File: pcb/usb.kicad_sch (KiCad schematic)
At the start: 8 parts, among them J2 Same Sky UJ20-C-H-G-SMT-P16-TR, U4 USBLC6-2SC6

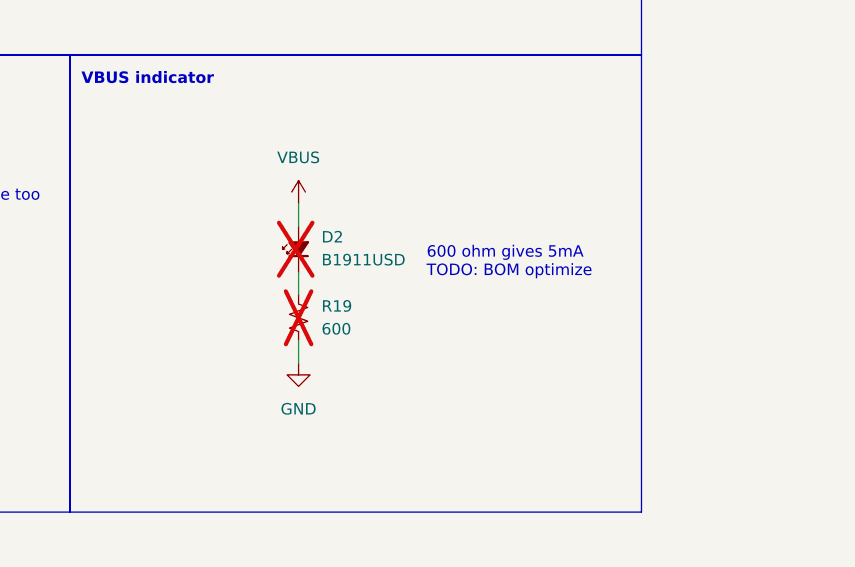
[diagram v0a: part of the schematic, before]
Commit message: Enabled and implemented VBUS LED
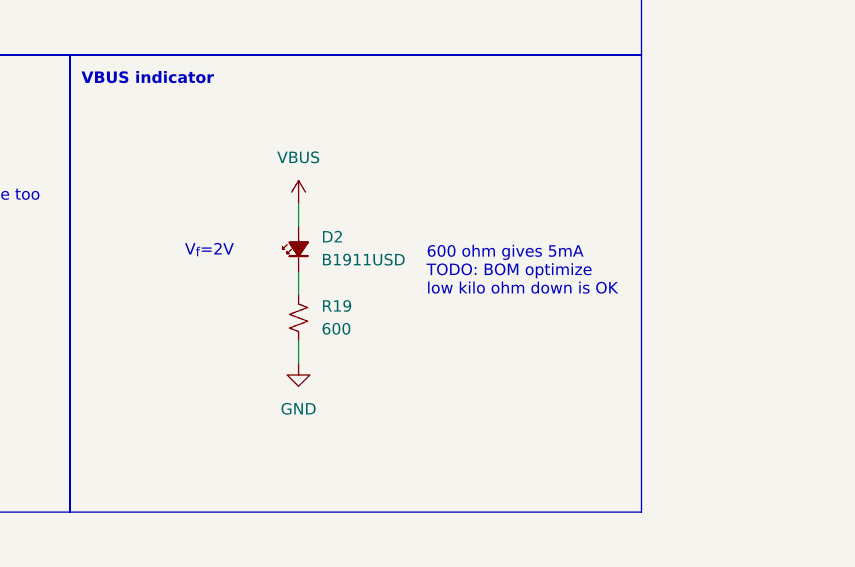
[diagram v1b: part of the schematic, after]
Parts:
- D2, R19: now fitted
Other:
- note added: "600 ohm gives 5mA TODO: BOM optimize low kilo ohm down is OK"
- note added: "V_{f}=2V"
- note removed: "600 ohm gives 5mA TODO: BOM optimize"
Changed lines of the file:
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@@
 		)
 	)
-	(text "600 ohm gives 5mA\nTODO: BOM optimize"
+	(text "600 ohm gives 5mA\nTODO: BOM optimize\nlow kilo ohm down is OK"
 		(exclude_from_sim no)
 		(at 103.124 122.936 0)
@@
 		(exclude_from_sim no)
 		(at 44.45 117.348 0)
+		(effects
+			(font
+				(size 1.27 1.27)
+			)
+		)
+	)
+	(text "V_{f}=2V"
+		(exclude_from_sim no)
+		(at 78.994 123.444 0)
 		(effects
 			(font
@@
 		(exclude_from_sim no)
 		(in_bom yes)
-		(on_board no)
-		(dnp yes)
+		(on_board yes)
+		(dnp no)
 		(fields_autoplaced yes)
 		(property "Reference" "R19"
@@
 		(exclude_from_sim no)
 		(in_bom yes)
-		(on_board no)
-		(dnp yes)
+		(on_board yes)
+		(dnp no)
 		(fields_autoplaced yes)
 		(property "Reference" "D2"

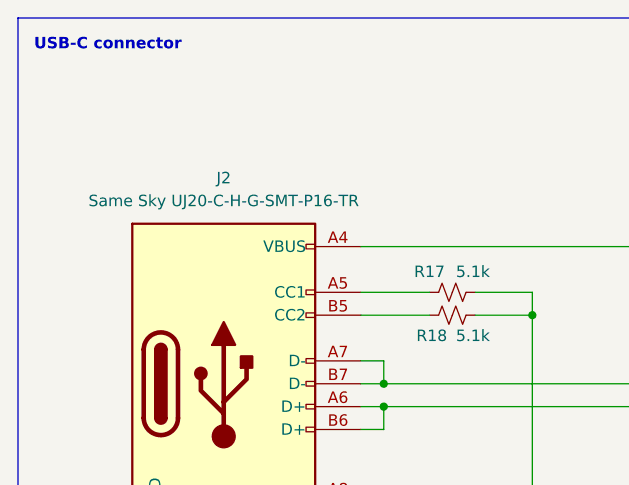
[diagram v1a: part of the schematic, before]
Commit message: Add MPN field for components except resistors
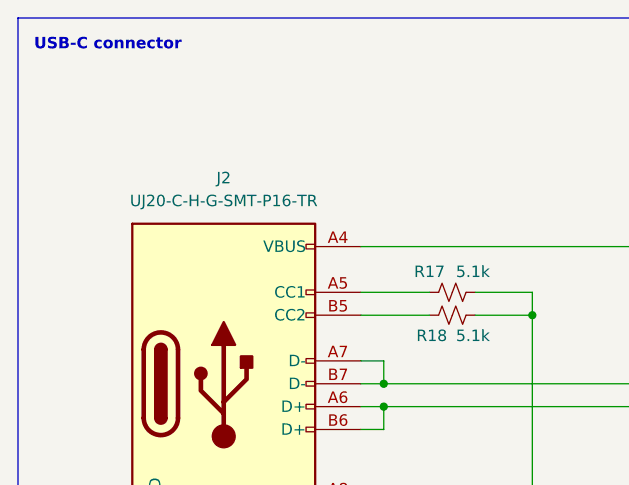
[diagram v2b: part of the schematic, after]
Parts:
- D2: MPN (none) -> B1911USD-20D000114U1930
- J2: value Same Sky UJ20-C-H-G-SMT-P16-TR -> UJ20-C-H-G-SMT-P16-TR; MPN (none) -> UJ20-C-H-G-SMT-P16-TR
- U4: MPN (none) -> USBLC6-2SC6
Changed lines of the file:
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@@
+			)
+		)
+		(property "MPN" ""
+			(at 88.9 130.81 0)
+			(effects
+				(font
+					(size 1.27 1.27)
+				)
+				(hide yes)
 			)
 		)
@@
 			)
 		)
+		(property "MPN" ""
+			(at 60.96 43.18 90)
+			(effects
+				(font
+					(size 1.27 1.27)
+				)
+				(hide yes)
+			)
+		)
 		(pin "1"
 		)
@@
 			)
 		)
+		(property "MPN" "B1911USD-20D000114U1930"
+			(at 88.9 123.19 90)
+			(effects
+				(font
+					(size 1.27 1.27)
+				)
+				(hide yes)
+			)
+		)
 		(pin "2"
 		)
@@
 			)
 		)
-		(property "Value" "Same Sky UJ20-C-H-G-SMT-P16-TR"
+		(property "Value" "UJ20-C-H-G-SMT-P16-TR"
 			(at 35.56 33.02 0)
 			(effects
@@
 			)
 		)
+		(property "MPN" "UJ20-C-H-G-SMT-P16-TR"
+			(at 35.56 53.34 0)
+			(effects
+				(font
+					(size 1.27 1.27)
+				)
+				(hide yes)
+			)
+		)
 		(pin "B6"
 		)
@@
 			)
 		)
+		(property "MPN" ""
+			(at 60.96 45.72 90)
+			(effects
+				(font
+					(size 1.27 1.27)
+				)
+				(hide yes)
+			)
+		)
 		(pin "1"
 		)
@@
 			)
 		)
+		(property "MPN" ""
+			(at 25.4 121.92 0)
+			(effects
+				(font
+					(size 1.27 1.27)
+				)
+				(hide yes)
+			)
+		)
 		(pin "2"
 		)
@@
 			)
 		)
+		(property "MPN" "USBLC6-2SC6"
+			(at 88.9 53.34 0)
+			(effects
+				(font
+					(size 1.27 1.27)
+				)
+				(hide yes)
+			)
+		)
 		(pin "6"
 		)
@@
 			(at 25.4 132.08 0)
 			(effects
+				(font
+					(size 1.27 1.27)
+				)
+				(hide yes)
+			)
+		)
+		(property "MPN" ""
+			(at 25.4 132.08 0)
+			(effects

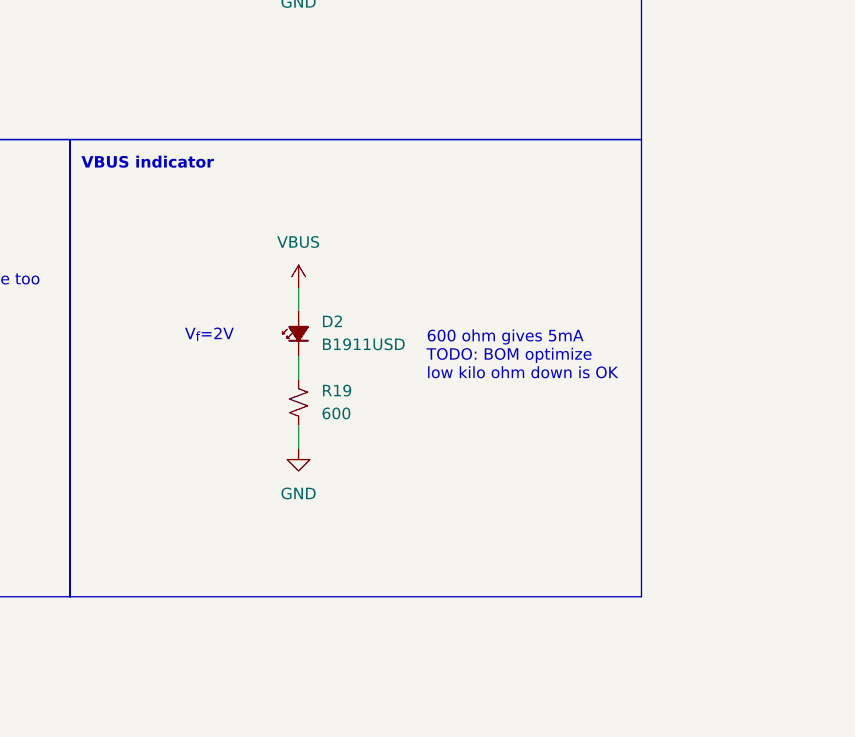
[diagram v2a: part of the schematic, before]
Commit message: BOM optimize VBUS LED
600R to 3x 150R = 450R for 6.667 mA
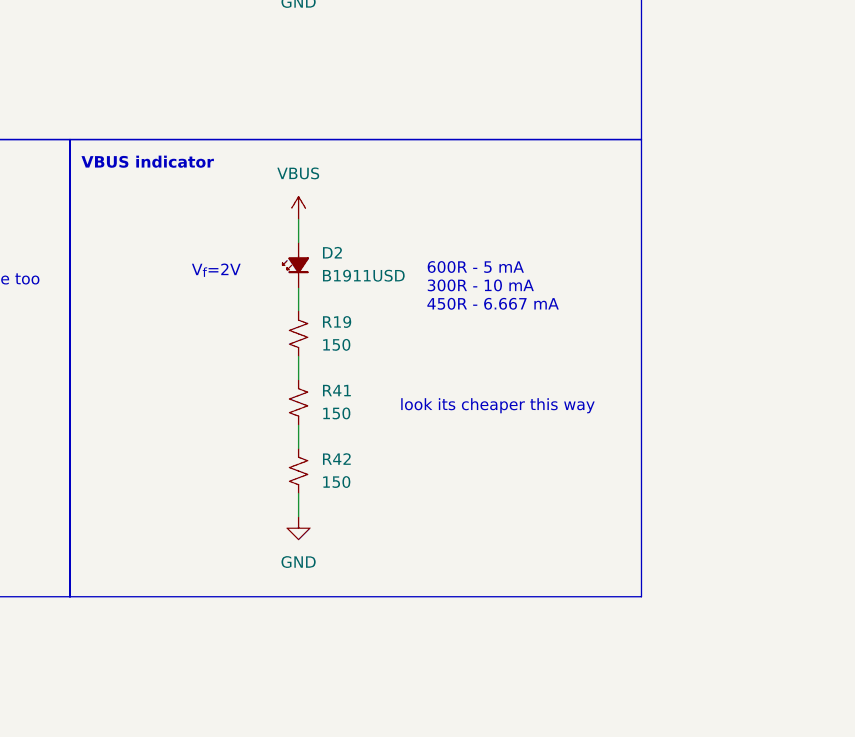
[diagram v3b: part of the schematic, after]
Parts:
- added R41, R42: 150, Resistor_SMD:R_0603_1608Metric, symbol Device:R_Small_US
- R19: value 600 -> 150
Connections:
- net GND: now also R42.2; no longer R19.2
- new net: R19.2, R41.1
- new net: R41.2, R42.1
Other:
- note added: "600R - 5 mA 300R - 10 mA 450R - 6.667 mA"
- note added: "look its cheaper this way"
- note removed: "600 ohm gives 5mA TODO: BOM optimize low kilo ohm down is OK"
- moved on the sheet: D2, R19

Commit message: Update resistor MPNs
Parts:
- R15: MPN (none) -> AC0603FR-0730KL
- R16: MPN (none) -> RC0603FR-0747KL
- R17, R18: MPN (none) -> RC0603FR-075K1L
- R19, R41, R42: MPN (none) -> RC0603JR-07150RL
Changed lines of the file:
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@@
 			)
 		)
-		(property "MPN" ""
+		(property "MPN" "RC0603JR-07150RL"
 			(at 88.9 123.19 0)
 			(effects
@@
 			)
 		)
-		(property "MPN" ""
+		(property "MPN" "RC0603FR-075K1L"
 			(at 60.96 43.18 90)
 			(effects
@@
 			)
 		)
-		(property "MPN" ""
+		(property "MPN" "RC0603FR-075K1L"
 			(at 60.96 45.72 90)
 			(effects
@@
 			)
 		)
-		(property "MPN" ""
+		(property "MPN" "AC0603FR-0730KL"
 			(at 25.4 121.92 0)
 			(effects
@@
 			)
 		)
-		(property "MPN" ""
+		(property "MPN" "RC0603JR-07150RL"
 			(at 88.9 130.81 0)
 			(effects
@@
 			)
 		)
-		(property "MPN" ""
+		(property "MPN" "RC0603JR-07150RL"
 			(at 88.9 138.43 0)
 			(effects
@@
 			)
 		)
-		(property "MPN" ""
+		(property "MPN" "RC0603FR-0747KL"
 			(at 25.4 132.08 0)
 			(effects

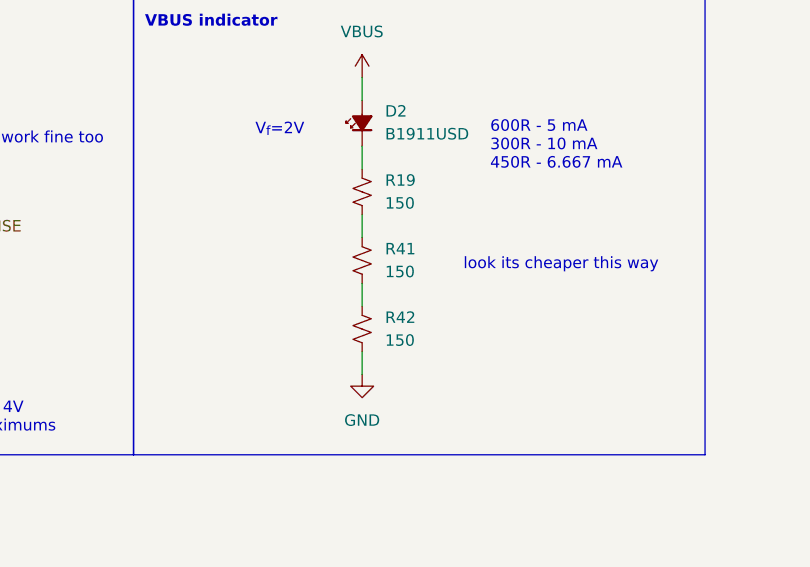
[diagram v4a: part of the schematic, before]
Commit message: Redo layout and routing for RGB LEDs
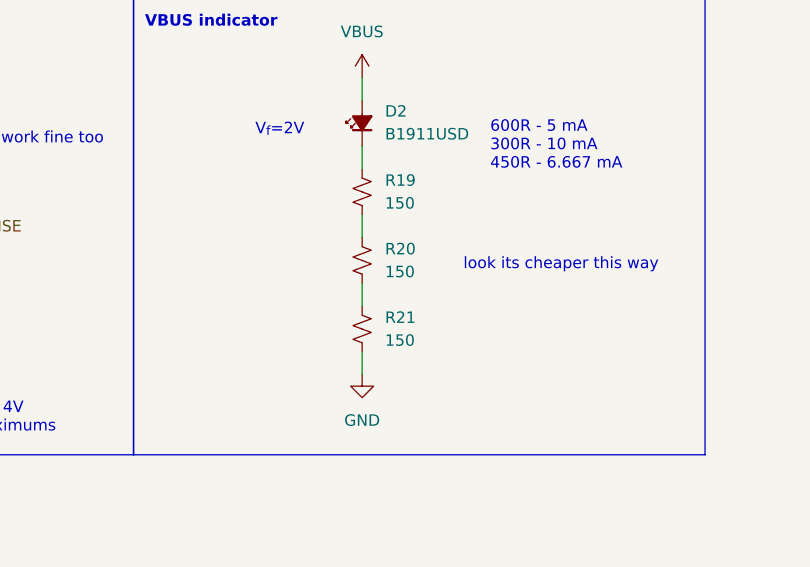
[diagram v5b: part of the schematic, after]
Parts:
- renumbered R41 to R20, R42 to R21
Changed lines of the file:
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@@
 		(dnp no)
 		(fields_autoplaced yes)
-		(property "Reference" "R41"
+		(property "Reference" "R20"
 			(at 91.44 129.5399 0)
 			(effects
@@
 			(project "airbrake_mod"
 				(path "/1f4fd4ed-9886-4375-a5ac-dc32d5760936/ca842921-3489-4085-9fee-8380a44600c3"
-					(reference "R41")
+					(reference "R20")
 					(unit 1)
 				)
@@
 		(dnp no)
 		(fields_autoplaced yes)
-		(property "Reference" "R42"
+		(property "Reference" "R21"
 			(at 91.44 137.1599 0)
 			(effects
@@
 			(project "airbrake_mod"
 				(path "/1f4fd4ed-9886-4375-a5ac-dc32d5760936/ca842921-3489-4085-9fee-8380a44600c3"
-					(reference "R42")
+					(reference "R21")
 					(unit 1)
 				)

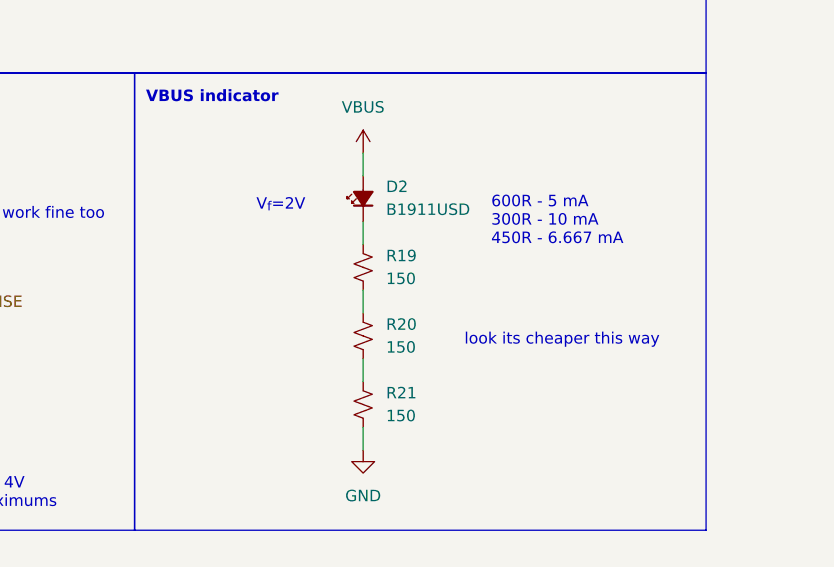
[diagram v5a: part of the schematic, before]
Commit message: Replace B1911USD LED with equivalent FC-1608SXK-620H08
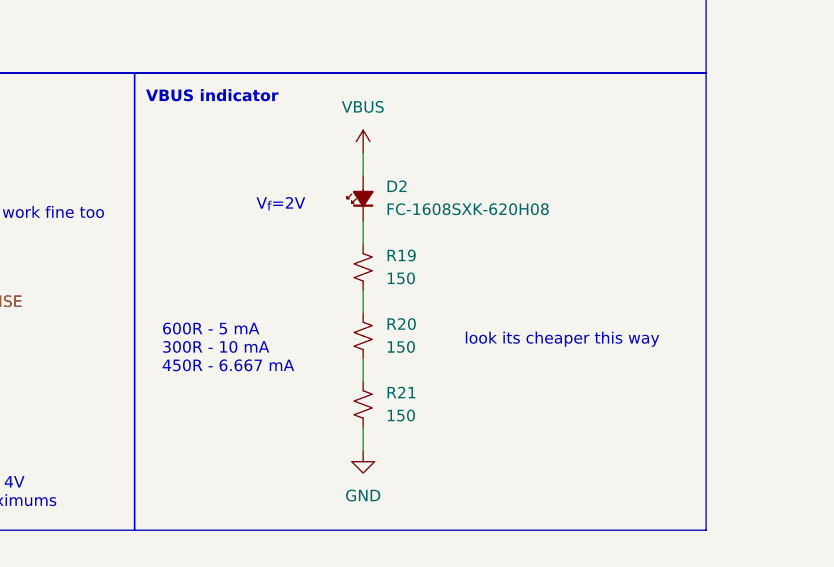
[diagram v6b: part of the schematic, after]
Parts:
- D2: value B1911USD -> FC-1608SXK-620H08; MPN B1911USD-20D000114U1930 -> FC-1608SXK-620H08
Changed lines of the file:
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@@
 	(text "600R - 5 mA\n300R - 10 mA\n450R - 6.667 mA"
 		(exclude_from_sim no)
-		(at 103.124 115.316 0)
+		(at 66.548 129.54 0)
 		(effects
 			(font
@@
 			)
 		)
-		(property "Value" "B1911USD"
+		(property "Value" "FC-1608SXK-620H08"
 			(at 91.44 116.7764 90)
 			(effects
@@
 			)
 		)
-		(property "MPN" "B1911USD-20D000114U1930"
+		(property "MPN" "FC-1608SXK-620H08"
 			(at 88.9 115.57 90)
 			(effects
